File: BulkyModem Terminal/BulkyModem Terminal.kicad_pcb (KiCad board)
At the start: 2 copper layers, 100 x 100 mm, 81 parts, among them J1 DC IN, J2 DCE, J3 Module_Panel, J5 C64_Modem_OUT, K1 HK19F-DC, M1 Mounting, M2 Mounting, M3 Mounting, M4 Mounting, SW1 SET_1200, U1 74HCT244, U2 74HCT04, U3 MAX232, U4 MAX232, U5 74HCT04, U6 74HCT32

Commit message: Part of a layout
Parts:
- removed A1: NodeMCU (v3), nodemcu_v3:NodeMCU-LoLinV3
- removed A2: Audio_Panel, BulkyModem:AudioModule
- removed C12, C13, C14, C15: 1uF, BulkyModem:CP_Radial_D4.0mm_P2.00mm_Custom
- removed C18, C8: 100nF, Capacitor_THT:C_Disc_D4.7mm_W2.5mm_P5.00mm
- removed D10: DCD, LED_THT:LED_D3.0mm
- removed D12: STANDBY, LED_THT:LED_D3.0mm
- removed D14: 1N4148, Diode_THT:D_DO-35_SOD27_P7.62mm_Horizontal
- removed JP10: INV_RX, solder_bridge:SolderJumper-3_P1.3mm_Open_RoundedPad1.0x1.5mm
- removed JP11: INV_CTS, solder_bridge:SolderJumper-3_P1.3mm_Open_RoundedPad1.0x1.5mm
- removed JP12: INV_DCD, solder_bridge:SolderJumper-3_P1.3mm_Open_RoundedPad1.0x1.5mm
- removed JP13: BYPASS, solder_bridge:SolderJumper-2_P1.3mm_Open_Pad1.0x1.5mm
- removed JP14: INV_RI, solder_bridge:SolderJumper-3_P1.3mm_Open_RoundedPad1.0x1.5mm
- removed JP15: TX_FILTER, solder_bridge:SolderJumper-3_P1.3mm_Open_RoundedPad1.0x1.5mm
- removed JP3: SEL_RxD, solder_bridge:SolderJumper-3_P1.3mm_Open_RoundedPad1.0x1.5mm
- removed JP4: SEL_TxD, solder_bridge:SolderJumper-3_P1.3mm_Open_RoundedPad1.0x1.5mm
- removed JP5: SEL_CTS, solder_bridge:SolderJumper-3_P1.3mm_Open_RoundedPad1.0x1.5mm
- removed JP6: SEL_RTS, solder_bridge:SolderJumper-3_P1.3mm_Open_RoundedPad1.0x1.5mm
- removed JP7: 232_SW, Connector_PinHeader_2.54mm:PinHeader_1x02_P2.54mm_Vertical
- removed JP8: INV_TX, solder_bridge:SolderJumper-3_P1.3mm_Open_RoundedPad1.0x1.5mm
- removed JP9: INV_RTS, solder_bridge:SolderJumper-3_P1.3mm_Open_RoundedPad1.0x1.5mm
- removed K1: HK19F-DC, HK19F-DC:HK19F-DC
- removed U4: MAX232, Package_DIP:DIP-16_W7.62mm_Socket_LongPads
- removed U6: 74HCT32, Package_DIP:DIP-14_W7.62mm_Socket_LongPads
- added C9: 100uF, Capacitor_THT:CP_Radial_D5.0mm_P2.50mm, F.Cu at (92.1, 104.8)
- added J4: VGA, VGA_DSUB:DSUB-15-L77HDE15SD1CH4F, F.Cu at (145.3, 48.0)
- added J6: PS/2_Connector, PS2_mini_din_6:MINI-DIN-6-FULL-SHIELD, F.Cu at (70.2, 88.7)
- added LS1: Speaker, small_buzzer:Buzzer_12x9.5RM7.6, F.Cu at (77.5, 109.2)
- added Q1: 2N3904, Package_TO_SOT_THT:TO-92_Inline_Wide, F.Cu at (95.9, 102.2)
- added R11: 1K, resistor:R_Axial_DIN0207_L6.3mm_D2.5mm_P10.16mm_Horizontal, F.Cu at (156.2, 78.1)
- added R13: 2k2, resistor:R_Axial_DIN0207_L6.3mm_D2.5mm_P10.16mm_Horizontal, F.Cu at (160.0, 78.1)
- added R20: 100, resistor:R_Axial_DIN0207_L6.3mm_D2.5mm_P10.16mm_Horizontal, F.Cu at (84.5, 137.8)
- added R22: 10k, resistor:R_Axial_DIN0207_L6.3mm_D2.5mm_P10.16mm_Horizontal, F.Cu at (149.2, 134.6)
- added R23: 2k2, resistor:R_Axial_DIN0207_L6.3mm_D2.5mm_P10.16mm_Horizontal, F.Cu at (155.6, 120.7)
- added R24: 2k2, resistor:R_Axial_DIN0207_L6.3mm_D2.5mm_P10.16mm_Horizontal, F.Cu at (159.4, 120.7)
- added R26: 220, resistor:R_Axial_DIN0207_L6.3mm_D2.5mm_P10.16mm_Horizontal, F.Cu at (84.5, 110.5)
- added R27: 2k, resistor:R_Axial_DIN0207_L6.3mm_D2.5mm_P10.16mm_Horizontal, F.Cu at (99.7, 91.4)
- added R28: 2k, resistor:R_Axial_DIN0207_L6.3mm_D2.5mm_P10.16mm_Horizontal, F.Cu at (99.7, 95.2)
- added R29: 120, resistor:R_Axial_DIN0207_L6.3mm_D2.5mm_P10.16mm_Horizontal, F.Cu at (113.0, 91.4)
- added R30: 120, resistor:R_Axial_DIN0207_L6.3mm_D2.5mm_P10.16mm_Horizontal, F.Cu at (113.0, 95.2)
- added R31: 10k, resistor:R_Axial_DIN0207_L6.3mm_D2.5mm_P10.16mm_Horizontal, F.Cu at (148.6, 116.2)
- added R32: 2k2, resistor:R_Axial_DIN0207_L6.3mm_D2.5mm_P10.16mm_Horizontal, F.Cu at (167.6, 116.2)
- added R5: 100, resistor:R_Axial_DIN0207_L6.3mm_D2.5mm_P10.16mm_Horizontal, F.Cu at (134.6, 67.9)
- added R6: 2k2, resistor:R_Axial_DIN0207_L6.3mm_D2.5mm_P10.16mm_Horizontal, F.Cu at (147.3, 78.1)
- added R7: 1K, resistor:R_Axial_DIN0207_L6.3mm_D2.5mm_P10.16mm_Horizontal, F.Cu at (143.5, 78.1)
- added R9: 470, resistor:R_Axial_DIN0207_L6.3mm_D2.5mm_P10.16mm_Horizontal, F.Cu at (139.7, 78.1)
- added SW2: DEFAULTS, Button_Switch_THT:SW_Tactile_SPST_Angled_PTS645Vx39-2LFS, F.Cu at (73.4, 133.4)
- D13: value STANDBY -> 3V3
- D2: value POWER -> 5V
- D3: value RI -> 1n4148; footprint LED_THT:LED_D3.0mm -> Diode_THT:D_DO-35_SOD27_P7.62mm_Horizontal
- D9: value C64 -> TTL
- J2: value DCE -> RS-232; footprint RND_DSUB:DSUB-9_Female_Horizontal_P2.77x2.84mm_EdgePinOffset7.70mm_Housed_MountingHolesOffset9.12mm -> RND_DSUB:DSUB-9_Male_Horizontal_P2.77x2.84mm_EdgePinOffset7.70mm_Housed_MountingHolesOffset9.12mm
- J3: footprint BulkyModem:Module_Panel -> BulkyModem:Terminal_Panel
- J5: value C64_Modem_OUT -> TTL; footprint BulkyModem:UserPort_Adapter_IDC -> Connector_PinHeader_2.54mm:PinHeader_1x06_P2.54mm_Horizontal; moved to B.Cu
- JP2: value BYPASS -> 232_SW; footprint solder_bridge:SolderJumper-2_P1.3mm_Open_Pad1.0x1.5mm -> Connector_PinHeader_2.54mm:PinHeader_1x02_P2.54mm_Vertical; moved to F.Cu
- R1, R2: value 2k2 -> 1K
- R15, R16: value 2k2 -> 100
- R17: value 2k -> 470
- R18: value 10k* -> 390
- R21: value 10k -> 100
- R25: value 2k2 -> 680
- R4: value 2k2* -> 2k2
- SW1: value SET_1200 -> RESET
- U1: value 74HCT244 -> Pico; footprint Package_DIP:DIP-20_W7.62mm_Socket_LongPads -> pi_pico:RPi_Pico_SMD_TH
- U2: value 74HCT04 -> 74HCT244; footprint Package_DIP:DIP-14_W7.62mm_Socket_LongPads -> Package_DIP:DIP-20_W7.62mm_Socket_LongPads
- moved D13 113.7 mm to (167.6, 130.2), turned to 180 degrees
- moved J5 104.0 mm to (87.2, 153.2), turned to -90 degrees
- moved C1 85.1 mm to (149.2, 129.5), turned to 90 degrees
- moved R3 83.0 mm to (163.2, 116.2), turned to -90 degrees
- moved D2 82.0 mm to (165.1, 135.3), turned to 0 degrees
- moved JP2 80.5 mm to (145.4, 134.6)
- moved C6 79.5 mm to (167.6, 113.0), turned to 180 degrees
- moved R1 73.5 mm to (144.8, 113.0), turned to 180 degrees
- moved R16 70.5 mm to (88.3, 137.8), turned to 90 degrees
- moved R15 69.2 mm to (80.6, 126.4)
- moved C7 64.0 mm to (82.5, 115.6)
- moved JP1 63.6 mm to (135.4, 134.6)
- moved D1 62.3 mm to (123.8, 113.0)
- moved G*** 58.5 mm to (37.5, 135.9)
- moved G*** 55.3 mm to (53.6, 80.6)
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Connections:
- net /Front Panel/LED_CTS renamed /Front Panel/LED.CTS
- net /Front Panel/LED_RTS renamed /Front Panel/LED.RTS
- net /Front Panel/LED_RX renamed /Front Panel/LED.RX
- net /Front Panel/LED_TX renamed /Front Panel/LED.TX
- C1 pad 1: VIN -> +5V
- C2 pad 1: unconnected-(U3-VS+-Pad2) -> Net-(U3-VS+)
- C3 pad 1: unconnected-(U3-C2+-Pad4) -> Net-(U3-C2+)
- C3 pad 2: unconnected-(U3-C2--Pad5) -> Net-(U3-C2-)
- C4 pad 2: unconnected-(U3-VS--Pad6) -> Net-(U3-VS-)
- C5 pad 1: unconnected-(U3-C1+-Pad1) -> Net-(U3-C1+)
- C5 pad 2: unconnected-(U3-C1--Pad3) -> Net-(U3-C1-)
- C6 pad 1: +5V -> +3.3V
- D1 pad 1: VIN -> Pico.RxD
- D1 pad 2: PWR_EN -> Net-(D1-A)
- D13 pad 1: /Front Panel/LED_STB -> Net-(D13-K)
- D13 pad 2: VSB -> +3.3V
- D2 pad 1: /Front Panel/LED_POW -> Net-(D2-K)
- D3 pad 1: /Front Panel/LED_RI -> Pico.CTS
- D3 pad 2: +5V -> Net-(D3-A)
- D8 pad 1: /Front Panel/LED_RS232 -> /Front Panel/LED.232
- D9 pad 1: /Front Panel/LED_C64 -> /Front Panel/LED.TTL
- J2 pad 1: /RS-232/SER_DCD -> unconnected-(J2-Pad1)
- J2 pad 2: /RS-232/DCE_TxD -> /Serial/DTE.RxD
- J2 pad 3: /RS-232/DCE_RxD -> /Serial/DTE.TxD
- J2 pad 4: Net-(JP13-B) -> unconnected-(J2-Pad4)
- J2 pad 6: Net-(JP13-B) -> unconnected-(J2-Pad6)
- J2 pad 7: /RS-232/DCE_CTS -> /Serial/DTE.RTS
- J2 pad 8: /RS-232/DCE_RTS -> /Serial/DTE.CTS
- J2 pad 9: /RS-232/SER_RI -> unconnected-(J2-Pad9)
- J3 pad 10: /Front Panel/LED_RI -> /Front Panel/LED.TTL
- J3 pad 11: /Front Panel/LED_RS232 -> unconnected-(J3-N.C.-Pad11)
- J3 pad 12: /Front Panel/LED_C64 -> unconnected-(J3-N.C.-Pad12)
- J3 pad 15: unconnected-(J3-N.C.-Pad15) -> DEFAULTS
- J3 pad 16: unconnected-(J3-N.C.-Pad16) -> RESET
- J3 pad 17: VSB -> VIN
- J3 pad 19: PWR_EN -> unconnected-(J3-N.C.-Pad19)
- J3 pad 3: /Front Panel/LED_POW -> /Front Panel/LED.POW
- J3 pad 4: /Front Panel/LED_STB -> unconnected-(J3-N.C.-Pad4)
- J3 pad 9: /Front Panel/LED_DCD -> /Front Panel/LED.232
- J5 pad 1: +5V -> TTL.RxD
- J5 pad 2: /C64_TX -> TTL.TxD
- J5 pad 3: /C64_RX -> TTL.CTS
- J5 pad 4: /C64_RTS -> TTL.RTS
- J5 pad 5: /C64_CTS -> +5V
- J5 pad 6: ESP_DCD -> GND
- JP1 pad 1: GND -> VIN
- JP1 pad 2: PWR_EN -> +5V
- JP2 pad 1: VIN -> GND
- JP2 pad 2: +5V -> MODE_SEL
- R1 pad 1: GND -> +3.3V
- R1 pad 2: Net-(D12-K) -> Net-(D1-A)
- R10 pad 1: ESP_TX -> unconnected-(U5-Pad8)
- R15 pad 1: MODE_232 -> Net-(U2-2A2)
- R15 pad 2: /Front Panel/LED_RS232 -> TTL.RxD
- R16 pad 1: MODE_C64 -> TTL.RTS
- R16 pad 2: /Front Panel/LED_C64 -> Net-(U2-2Y1)
- R17 pad 1: GND -> G2
- R17 pad 2: Net-(A1-D1) -> /VGA/VGA.G
- R18 pad 1: +3.3V -> B1
- R18 pad 2: Net-(A1-RX) -> /VGA/VGA.B
- R19 pad 1: ESP_CTS -> B0
- R19 pad 2: Net-(A1-D1) -> /VGA/VGA.B
- R2 pad 1: unconnected-(U5-Pad10) -> +3.3V
- R2 pad 2: /Front Panel/LED_RI -> Net-(D3-A)
- R21 pad 1: MODE_SEL -> Net-(U2-2A3)
- R21 pad 2: +5V -> TTL.CTS
- R25 pad 1: unconnected-(U5-Pad8) -> Net-(Q1-B)
- R25 pad 2: /Front Panel/LED_DCD -> BUZZER
- R3 pad 2: /Front Panel/LED_STB -> Net-(D2-K)
- R4 pad 2: /Front Panel/LED_POW -> /Front Panel/LED.POW
- R8 pad 1: ESP_RX -> unconnected-(U5-Pad10)
- SW1 pad 1: Net-(A1-D0) -> GND
- SW1 pad 2: GND -> RESET
- U1 pad 1: MODE_232 -> B0
- U1 pad 10: GND -> R2
- U1 pad 11: /C64_CTS -> SYNC
- U1 pad 12: ESP_CTS -> BUZZER
- U1 pad 13: /C64_RX -> GND
- U1 pad 14: ESP_RX -> PS2.DAT
- U1 pad 15: ESP_RTS -> PS2.CLK
- U1 pad 16: /232_RTS -> unconnected-(U1-GPIO12-Pad16)_0
- U1 pad 17: ESP_TX -> unconnected-(U1-GPIO13-Pad17)_0
- U1 pad 18: /232_TX -> GND
- U1 pad 19: MODE_C64 -> unconnected-(U1-GPIO14-Pad19)
- U1 pad 2: ESP_TX -> B1
- U1 pad 20: +5V -> unconnected-(U1-GPIO15-Pad20)_0
- U1 pad 3: /C64_TX -> GND
- U1 pad 4: ESP_RTS -> G0
- U1 pad 5: /C64_RTS -> G1
- U1 pad 6: /232_RX -> G2
- U1 pad 7: ESP_RX -> R0
- U1 pad 8: /232_CTS -> GND
- U1 pad 9: ESP_CTS -> R1
- U2 pad 1: ESP_RI -> MODE_232
- U2 pad 10: Net-(JP11-A) -> GND
- U2 pad 11: Net-(JP11-B) -> Net-(U2-2A3)
- U2 pad 12: Net-(JP12-A) -> Pico.CTS
- U2 pad 13: ESP_DCD -> Net-(U2-2A2)
- U2 pad 14: +5V -> Pico.RxD
- U2 pad 2: Net-(JP14-A) -> Pico.TxD
- U2 pad 3: /232_TX -> Net-(U2-2Y0)
- U2 pad 4: Net-(JP8-B) -> Pico.RTS
- U2 pad 5: /232_RTS -> Net-(U2-2Y1)
- U2 pad 6: Net-(JP9-A) -> 232.RxD
- U2 pad 7: GND -> Pico.RxD
- U2 pad 8: Net-(JP10-B) -> 232.CTS
- U2 pad 9: Net-(JP10-A) -> Pico.CTS
- U3 pad 1: unconnected-(U3-C1+-Pad1) -> Net-(U3-C1+)
- U3 pad 10: Net-(JP9-C) -> 232.TxD
- U3 pad 11: Net-(JP8-C) -> 232.RTS
- U3 pad 12: Net-(JP10-A) -> 232.RxD
- U3 pad 13: /RS-232/SER_RxD -> /Serial/DTE.RxD
- U3 pad 14: /RS-232/SER_TxD -> /Serial/DTE.RTS
- U3 pad 2: unconnected-(U3-VS+-Pad2) -> Net-(U3-VS+)
- U3 pad 3: unconnected-(U3-C1--Pad3) -> Net-(U3-C1-)
- U3 pad 4: unconnected-(U3-C2+-Pad4) -> Net-(U3-C2+)
- U3 pad 5: unconnected-(U3-C2--Pad5) -> Net-(U3-C2-)
- U3 pad 6: unconnected-(U3-VS--Pad6) -> Net-(U3-VS-)
- U3 pad 7: /RS-232/SER_RTS -> /Serial/DTE.TxD
- U3 pad 8: /RS-232/SER_CTS -> /Serial/DTE.CTS
- U3 pad 9: Net-(JP11-B) -> 232.CTS
- U5 pad 11: ESP_RI -> Pico.RxD
- U5 pad 13: MODE_C64 -> MODE_TTL
- U5 pad 2: MODE_C64 -> MODE_TTL
- U5 pad 3: ESP_RTS -> Pico.RTS
- U5 pad 5: ESP_CTS -> Pico.CTS
- U5 pad 9: ESP_DCD -> Pico.TxD
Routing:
- net ESP_TX: track 197.4 -> 0.00 mm, vias 5 -> 0
- net ESP_RX: track 184.5 -> 0.00 mm, vias 4 -> 0
- net PWR_EN: track 168.7 -> 0.00 mm, vias 2 -> 0
- net VSB: track 166.2 -> 0.00 mm, vias 4 -> 0
- net DEFAULTS: track 0.00 -> 150.9 mm
- net ESP_DCD: track 140.3 -> 0.00 mm, vias 5 -> 0
- net Net-(A1-D4): track 137.4 -> 0.00 mm, vias 3 -> 0
- net RESET: track 0.00 -> 137.0 mm
- net ESP_RI: track 118.2 -> 0.00 mm, vias 3 -> 0
- net Net-(A1-D5): track 117.9 -> 0.00 mm, vias 3 -> 0
- net Net-(A1-D0): track 114.4 -> 0.00 mm, vias 2 -> 0
- net MODE_C64: track 114.1 -> 0.00 mm, vias 2 -> 0
- net /Front Panel/LED_STB: track 110.7 -> 0.00 mm, vias 3 -> 0
- net ESP_RTS: track 100.0 -> 0.00 mm, vias 4 -> 0
- net /RS-232/DCE_CTS: track 99.2 -> 0.00 mm
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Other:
- board text added: "GND"
- board text added: "POW"
- board text added: "RxD"
- board text added: "Terminal (rev. A) github.com/tebl"
- board text added: "TxD"
- board text added: "VCC"
- board text removed: "A2"
- board text removed: "C64"
- board text removed: "DCD"
- board text removed: "Do not install"
- board text removed: "Link JP13 if not installing U4"
- board text removed: "Link JP2 if not installing K1"
- board text removed: "Module (rev. E) github.com/tebl"
- board text removed: "Power"
- board text removed: "RI"
- board text removed: "RS232"

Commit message: Added remaining tracks
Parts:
- G***: renamed from REF***; footprint Symbols:KiCad-Logo2_6mm_SilkScreen -> Symbol:KiCad-Logo2_6mm_SilkScreen
- G***: moved to F.Cu
- G***: moved to B.Cu
- moved G*** 114.9 mm to (144.1, 93.3), turned to 180 degrees
- moved G*** 86.2 mm to (138.4, 95.9), turned to 0 degrees
- moved G*** 77.3 mm to (123.2, 71.8)
- moved Q1 1.27 mm to (97.2, 102.2)
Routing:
- net MODE_TTL: track 33.9 -> 88.0 mm, vias 0 -> 1
- net MODE_232: track 25.7 -> 77.9 mm, vias 0 -> 2
- net unconnected-(U5-Pad10): track 0.00 -> 46.5 mm
- net Pico.RTS: track 50.9 -> 92.2 mm, vias 2 -> 4
- net +5V: track 517.0 -> 556.1 mm, vias 4 -> 5
- net Pico.TxD: track 34.7 -> 71.4 mm, vias 0 -> 1
- net unconnected-(U5-Pad8): track 0.00 -> 27.9 mm
- net Pico.CTS: track 49.6 -> 77.3 mm, vias 0 -> 1
- net Pico.RxD: track 20.2 -> 44.0 mm, vias 0 -> 1
- net unconnected-(U5-Pad4): track 0.00 -> 16.5 mm, vias 0 -> 1
- net Net-(Q1-B): track 14.0 -> 15.3 mm
- net DEFAULTS: track 150.9 -> 150.1 mm
- net 232.RTS: track 49.2 -> 48.4 mm
- net Net-(J6-Pad5): track 24.6 -> 23.9 mm
- net /Front Panel/LED.TX: track 23.3 -> 22.7 mm
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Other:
- board text added: "<"
- board text added: ">"

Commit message: Exported files
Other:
- board text added: "232"
- board text added: "3V3"
- board text added: "5V"
- board text added: "TTL"
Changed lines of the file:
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@@
 		(tags "9-pin D-Sub connector horizontal angled 90deg THT male pitch 2.77x2.84mm pin-PCB-offset 7.699999999999999mm mounting-holes-distance 25mm mounting-hole-offset 25mm")
 		(property "Reference" "J2"
-			(at 5.54 -2.8 180)
+			(at 18.065 5.08 180)
 			(layer "F.SilkS")
-			(hide yes)
 			(effects
 				(font
@@
 		(tags "Resistor Axial_DIN0207 series Axial Horizontal pin pitch 10.16mm 0.25W = 1/4W length 6.3mm diameter 2.5mm")
 		(property "Reference" "R28"
-			(at 3.175 0 -90)
+			(at 6.985 0 -90)
 			(layer "F.SilkS")
 			(effects
@@
 		)
 		(property "Value" "2k"
-			(at 6.35 0 180)
+			(at 3.81 0 180)
 			(layer "F.SilkS")
 			(effects
@@
 		(tags "Resistor Axial_DIN0207 series Axial Horizontal pin pitch 10.16mm 0.25W = 1/4W length 6.3mm diameter 2.5mm")
 		(property "Reference" "R30"
-			(at 3.175 0 -90)
+			(at 6.985 0 -90)
 			(layer "F.SilkS")
 			(effects
@@
 		)
 		(property "Value" "120"
-			(at 6.35 0 180)
+			(at 3.81 0 180)
 			(layer "F.SilkS")
 			(effects
@@
 		)
 		(property "Value" "2k2"
-			(at 6.35 0 90)
+			(at 6.985 0.635 90)
 			(layer "F.SilkS")
 			(effects
 				(font
-					(size 1 1)
-					(thickness 0.15)
+					(size 0.8 0.8)
+					(thickness 0.1)
 				)
+				(justify left)
 			)
 		)
@@
 		)
 		(property "Value" "2k2"
-			(at 6.35 0 90)
+			(at 6.985 0.635 90)
 			(layer "F.SilkS")
 			(effects
 				(font
-					(size 1 1)
-					(thickness 0.15)
+					(size 0.8 0.8)
+					(thickness 0.1)
 				)
+				(justify left)
 			)
 		)
@@
 		(tags "Resistor Axial_DIN0207 series Axial Horizontal pin pitch 10.16mm 0.25W = 1/4W length 6.3mm diameter 2.5mm")
 		(property "Reference" "R27"
-			(at 3.175 0 -90)
+			(at 6.985 0 -90)
 			(layer "F.SilkS")
 			(effects
@@
 		)
 		(property "Value" "2k"
-			(at 6.35 0 180)
+			(at 3.81 0 180)
 			(layer "F.SilkS")
 			(effects
@@
 			(effects
 				(font
-					(size 1 1)
-					(thickness 0.15)
+					(size 0.8 0.8)
+					(thickness 0.1)
 				)
 			)
@@
 		)
 		(property "Value" "RESET"
-			(at 2.25 5.38988 -90)
-			(layer "F.Fab")
+			(at 7.64 0.9225 0)
+			(layer "F.SilkS")
 			(effects
 				(font
-					(size 1 1)
-					(thickness 0.15)
+					(size 0.8 0.8)
+					(thickness 0.1)
 				)
 			)
@@
 		(tags "15-pin D-Sub connector horizontal angled 90deg THT female pitch 2.29x1.98mm pin-PCB-offset 3.0300000000000002mm mounting-holes-distance 25mm mounting-hole-offset 25mm")
 		(property "Reference" "J4"
-			(at 10.2 17.43 180)
+			(at -12.581 7.874 180)
 			(layer "F.SilkS")
 			(effects
@@
 		)
 		(property "Value" "2k2"
-			(at 6.35 0 90)
+			(at 6.985 0.635 90)
 			(layer "F.SilkS")
 			(effects
 				(font
-					(size 1 1)
-					(thickness 0.15)
+					(size 0.8 0.8)
+					(thickness 0.1)
 				)
+				(justify left)
 			)
 		)
@@
 		)
 		(property "Value" "DEFAULTS"
-			(at 2.25 5.38988 -90)
-			(layer "F.Fab")
+			(at -3.155 0.9225 0)
+			(layer "F.SilkS")
 			(effects
 				(font
-					(size 1 1)
-					(thickness 0.15)
+					(size 0.8 0.8)
+					(thickness 0.1)
 				)
 			)
@@
 		(tags "Resistor Axial_DIN0207 series Axial Horizontal pin pitch 10.16mm 0.25W = 1/4W length 6.3mm diameter 2.5mm")
 		(property "Reference" "R25"
-			(at 3.175 0 0)
+			(at 6.985 0 0)
 			(layer "F.SilkS")
 			(effects
@@
 		)
 		(property "Value" "680"
-			(at 6.35 0 -90)
+			(at 3.81 0 -90)
 			(layer "F.SilkS")
 			(effects
@@
 		)
 		(property "Value" "2k2"
-			(at 6.35 0 90)
+			(at 6.985 0.635 90)
 			(layer "F.SilkS")
 			(effects
 				(font
-					(size 1 1)
-					(thickness 0.15)
+					(size 0.8 0.8)
+					(thickness 0.1)
 				)
+				(justify left)
 			)
 		)
@@
 		(tags "Resistor Axial_DIN0207 series Axial Horizontal pin pitch 10.16mm 0.25W = 1/4W length 6.3mm diameter 2.5mm")
 		(property "Reference" "R29"
-			(at 3.175 0 -90)
+			(at 6.985 0 -90)
 			(layer "F.SilkS")
 			(effects
@@
 		)
 		(property "Value" "120"
-			(at 6.35 0 180)
+			(at 3.81 0 180)
 			(layer "F.SilkS")
 			(effects
@@
 	)
 	(gr_text "TX"
-		(at 114.3 131.445 0)
+		(at 113.03 131.445 0)
 		(layer "F.SilkS")
 		(effects
@@
 		)
 	)
-	(gr_text "Standby"
-		(at 67.31 133.985 90)
+	(gr_text "5V"
+		(at 163.83 123.19 90)
 		(layer "F.SilkS")
 		(effects
@@
 	)
 	(gr_text "POW"
-		(at 100.965 131.445 0)
+		(at 100.33 131.445 0)
 		(layer "F.SilkS")
 		(effects
@@
 		(layer "F.SilkS")
 		(effects
+			(font
+				(size 0.8 0.8)
+				(thickness 0.1)
+			)
+			(justify left)
+		)
+	)
+	(gr_text "TTL"
+		(at 160.02 127.635 90)
+		(layer "F.SilkS")
+		(effects
+			(font
+				(size 0.8 0.8)
+				(thickness 0.1)
+			)
+			(justify left)
+		)
+	)
+	(gr_text "3V3"
+		(at 168.275 123.19 90)
+		(layer "F.SilkS")
+		(effects
+			(font
+				(size 0.8 0.8)
+				(thickness 0.1)
+			)
+			(justify left)
+		)
+	)
+	(gr_text "232"
+		(at 156.21 127.635 90)
+		(layer "F.SilkS")
+		(effects

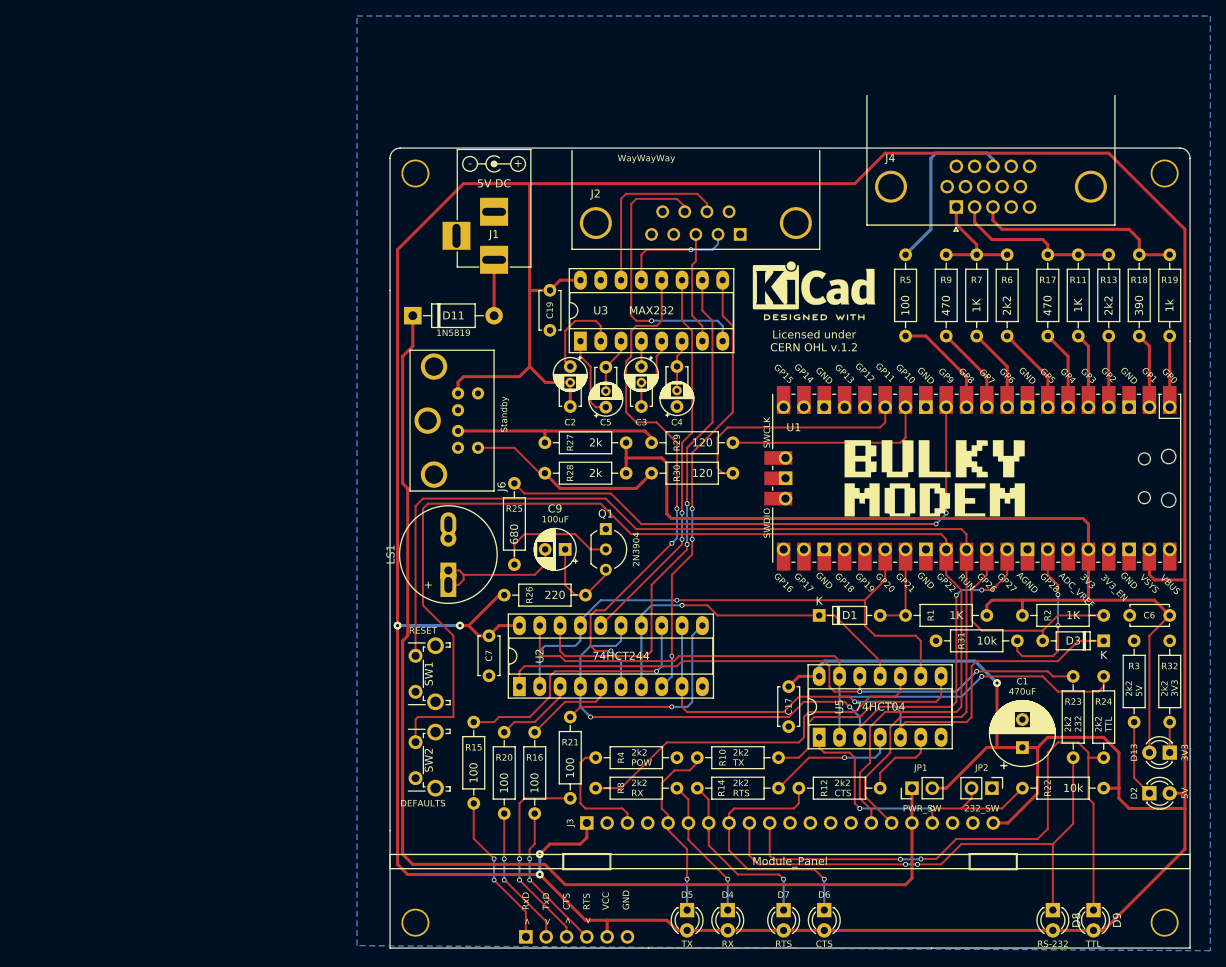
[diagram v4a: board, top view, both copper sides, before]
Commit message: Change PS/2 circuit
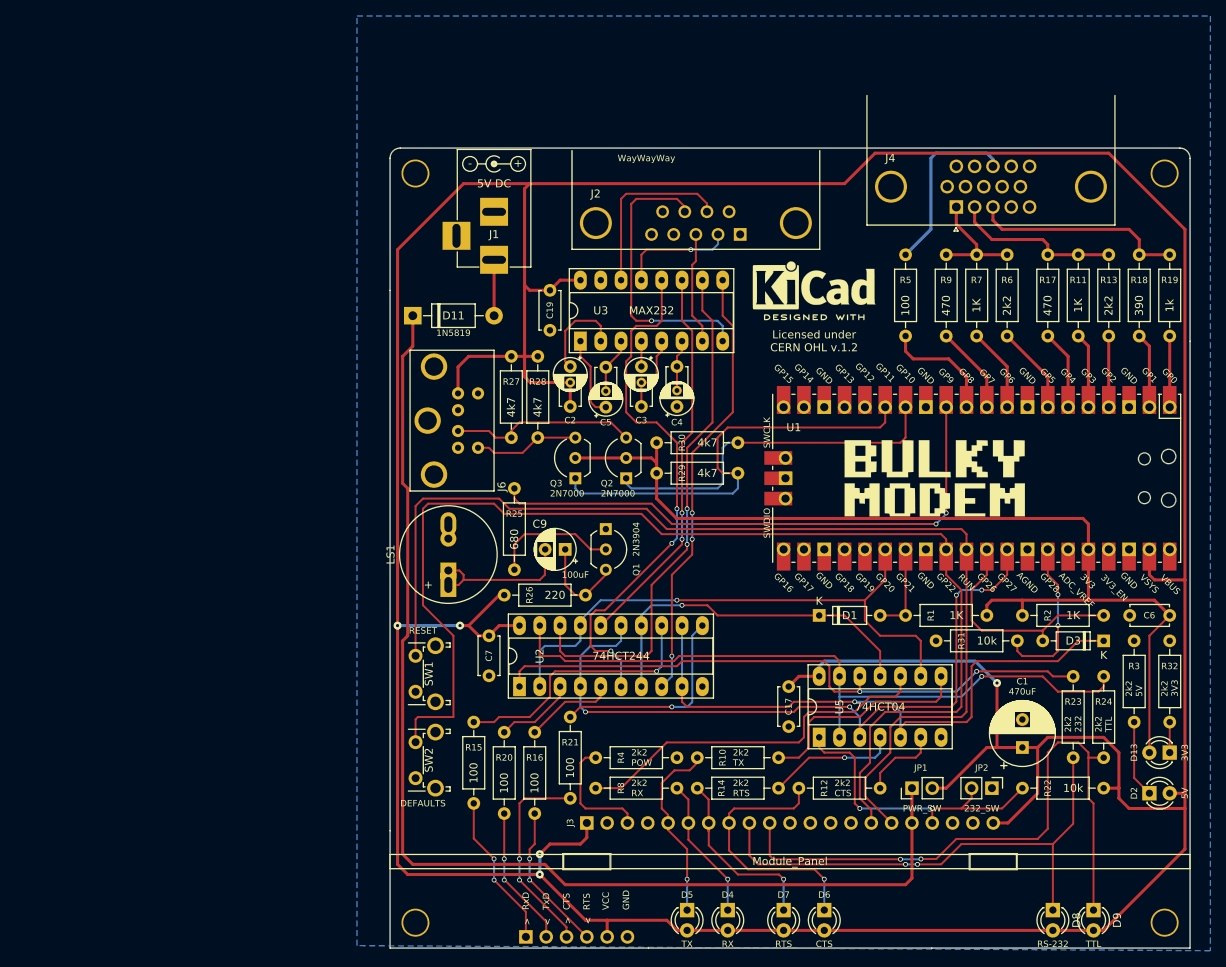
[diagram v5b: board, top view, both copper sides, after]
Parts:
- added Q2: 2N7000, Package_TO_SOT_THT:TO-92_Inline_Wide, F.Cu at (99.7, 95.9)
- added Q3: 2N7000, Package_TO_SOT_THT:TO-92_Inline_Wide, F.Cu at (93.3, 95.9)
- R27, R28: value 2k -> 4k7
- R29, R30: value 120 -> 4k7
- moved R28 18.3 mm to (88.6, 80.6), turned to -90 degrees
- moved R27 18.0 mm to (85.3, 80.6), turned to -90 degrees
- moved R29 10.3 mm to (103.5, 95.2), turned to 0 degrees
- moved R30 10.3 mm to (103.5, 91.4), turned to 0 degrees
- moved R25 0.63 mm to (85.7, 107.3)
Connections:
- J2 pad 0: (no net) -> GND
- J6 pad 1: Net-(J6-Pad1) -> Net-(Q2-D)
- J6 pad 5: Net-(J6-Pad5) -> Net-(Q3-D)
- R27 pad 1: +3.3V -> +5V
- R27 pad 2: Net-(J6-Pad1) -> Net-(Q2-D)
- R28 pad 1: +3.3V -> +5V
- R28 pad 2: Net-(J6-Pad5) -> Net-(Q3-D)
- R29 pad 1: PS2.DAT -> +3.3V
- R29 pad 2: Net-(J6-Pad1) -> PS2.CLK
- R30 pad 1: PS2.CLK -> +3.3V
- R30 pad 2: Net-(J6-Pad5) -> PS2.DAT
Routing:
- net Net-(J6-Pad1): track 26.6 -> 0.00 mm
- net PS2.CLK: track 29.6 -> 54.3 mm
- net Net-(J6-Pad5): track 23.9 -> 0.00 mm
- net Net-(Q2-D): track 0.00 -> 23.5 mm
- net PS2.DAT: track 25.7 -> 44.9 mm
- net Net-(Q3-D): track 0.00 -> 13.2 mm
- net +5V: track 556.1 -> 561.3 mm
- net +3.3V: track 123.5 -> 127.5 mm
- net Pico.CTS: track 77.3 -> 75.9 mm
- net SYNC: track 13.5 -> 14.7 mm
- net Pico.RTS: track 92.2 -> 91.2 mm
- net Net-(C9-Pad2): track 19.3 -> 20.4 mm
- net Pico.RxD: track 44.0 -> 44.8 mm
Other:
- board text added: "Terminal (rev. B) github.com/tebl"
- board text removed: "Standby"
- board text removed: "Terminal (rev. A) github.com/tebl"
